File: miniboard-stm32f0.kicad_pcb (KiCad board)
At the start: 2 copper layers, 44 x 18.5 mm, 21 parts, among them P1 CONN_01X02, P2 CONN_01X13, P3 CONN_01X01, SW1 SW_PUSH, SW2 SW_PUSH, U1 stm32f030f4p6, Y1 8MHz

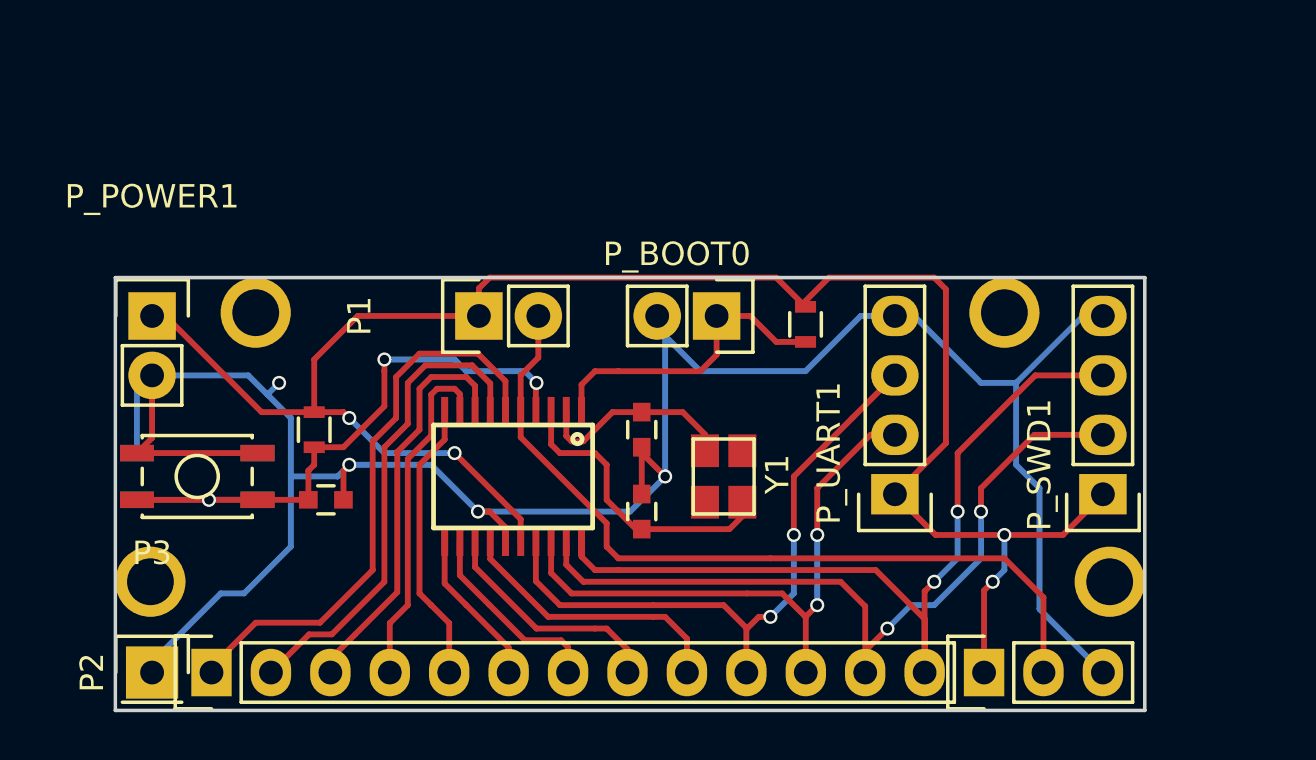
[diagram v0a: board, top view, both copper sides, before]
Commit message: Change quartz footprint, add text
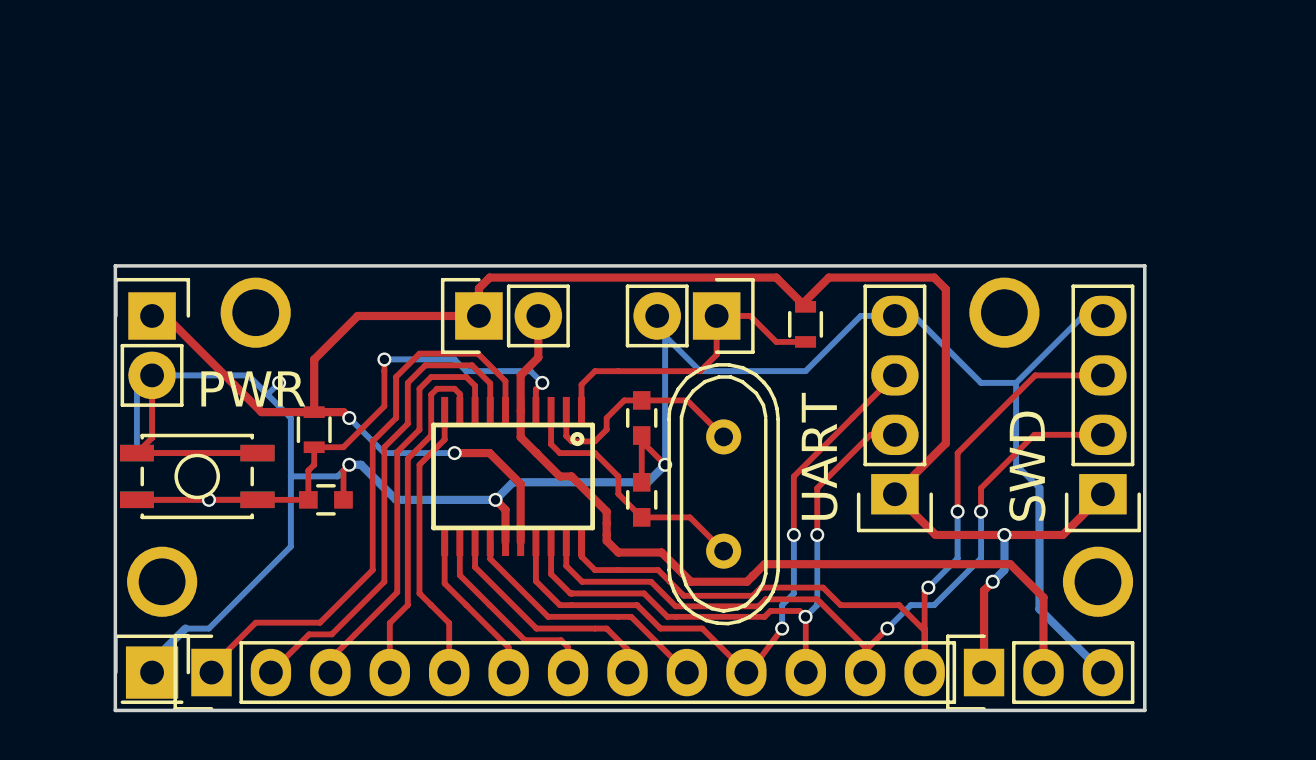
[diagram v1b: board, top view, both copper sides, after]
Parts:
- Y1: footprint Crystals:crystal_FA238-TSX3225 -> Crystals:Crystal_HC49-U_Vertical
- moved Y1 0.75 mm to (140.0, 111.8)
- moved C1 0.50 mm to (136.5, 108.5)
- moved C2 0.50 mm to (136.5, 112.0)
- moved H2 0.50 mm to (156.0, 115.5)
- moved H4 0.50 mm to (116.0, 115.5)
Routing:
- net /OSC_OUT: track 13.4 -> 11.4 mm
- net +3V3: track 79.4 -> 80.2 mm
- net /OSC_IN: track 8.70 -> 9.56 mm
- net /PB1: track 12.0 -> 11.1 mm
- net VAA: track 34.5 -> 35.2 mm
- net /PA13_SWDIO: track 35.3 -> 34.6 mm
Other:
- board size 44 x 18.5 mm -> 44 x 19 mm
- net class power added: clearance 0.2, trace_width 0.35, via_dia 0.6, via_drill 0.4
- board text added: "3.3"
- board text added: "3.3 VDD"
- board text added: "3.3V"
- board text added: "BOOT0"
- board text added: "FLASH"
- board text added: "GND"
- board text added: "PA0"
- board text added: "PA1"
- board text added: "PA10"
- board text added: "PA13"
- board text added: "PA14"
- board text added: "PA2"
- board text added: "PA3"
- board text added: "PA4"
- board text added: "PA5"
- board text added: "PA6"
- board text added: "PA7"
- board text added: "PA9"
- board text added: "PB1"
- board text added: "PWR"
- board text added: "RAM"
- board text added: "RST"
- board text added: "RX"
- board text added: "SWCLK"
- board text added: "SWD"
- board text added: "SWDIO"
- board text added: "TX"
- board text added: "UART"
- board text added: "VDDA"

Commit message: Add oshw logo Generate missing gerber files
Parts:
- added G***: LOGO, oshw:logo_xs, F.Cu at (124.2, 105.9)
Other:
- board text removed: "PWR"

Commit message: move logo
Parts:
- moved G*** 1.37 mm to (124.7, 104.6)
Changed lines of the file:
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@@
     (links 51)
     (no_connects 0)
-    (area 113.924999 101.924999 158.075001 121.075001)
+    (area 110.461667 97.915 161.318334 126.393095)
     (thickness 1.6)
     (drawings 46)
@@
   )
   (module oshw:logo_xs (layer F.Cu)
-    (at 124.206 105.918)
+    (at 124.714 104.648)
     (fp_text reference G*** (at 0 0) (layer F.SilkS) hide
       (effects (font (thickness 0.3)))

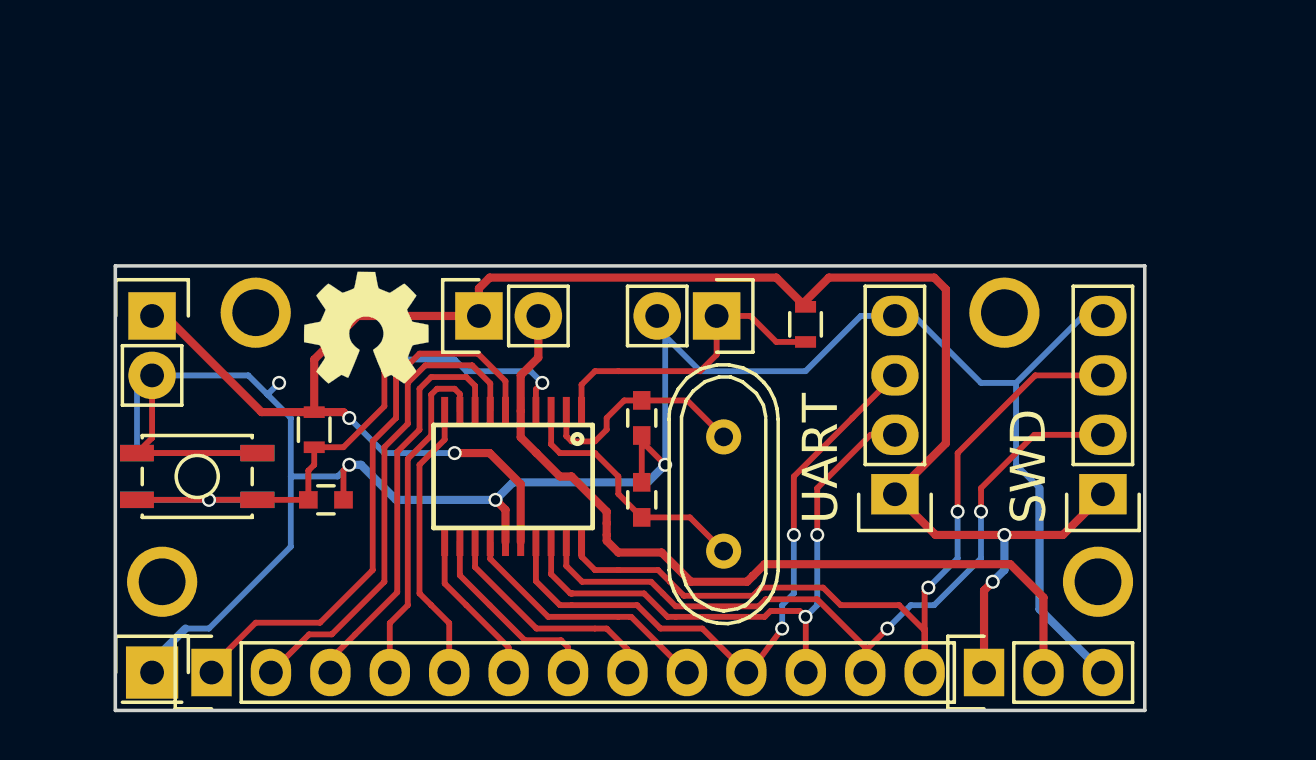
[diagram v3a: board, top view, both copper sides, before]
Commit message: * Use edge connector for SWD and uart connector * Add power LED * Fix reset button footprint * Add decoupling caps * Realign power connector
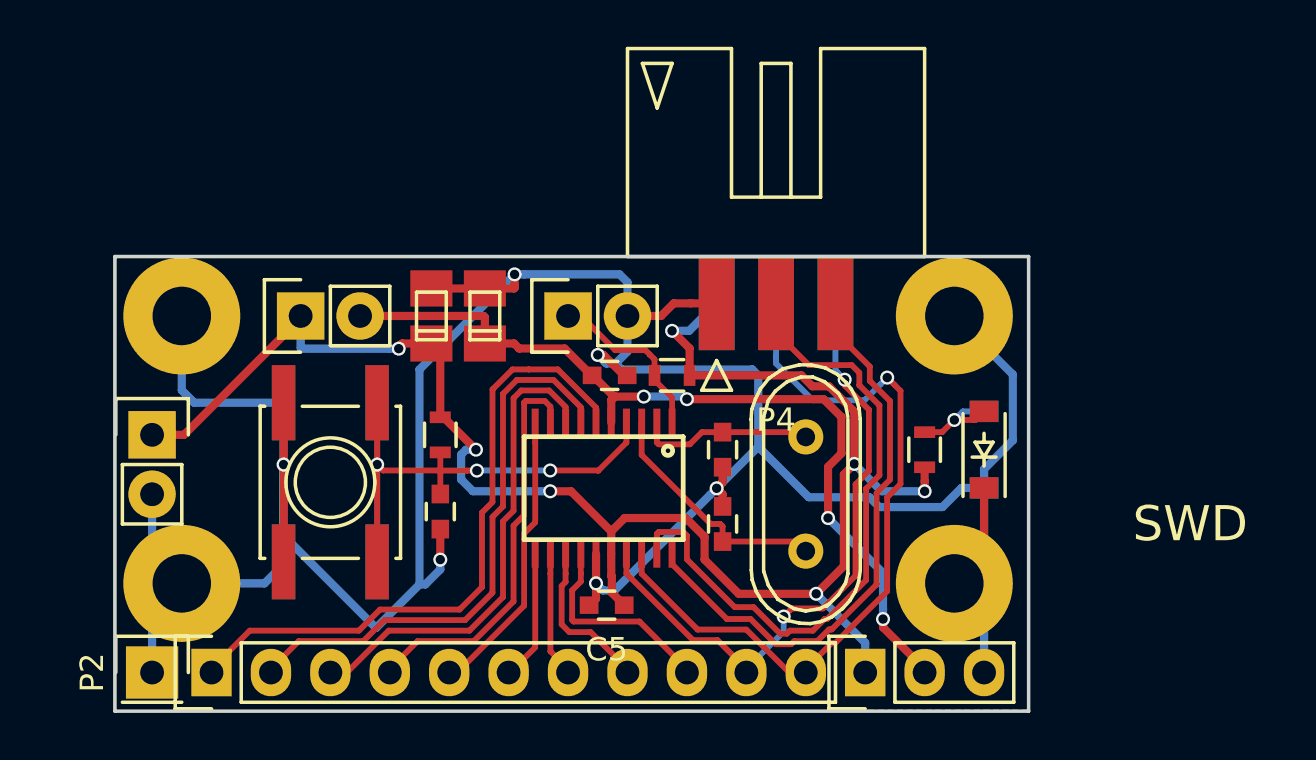
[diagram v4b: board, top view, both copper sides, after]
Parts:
- removed G***: LOGO, oshw:logo_xs
- removed P_SWD1, P_UART1: CONN_01X04, Pin_Headers:Pin_Header_Straight_1x04
- added C4: 4.7uF, Capacitors_Tantalum_SMD:TantalC_SizeR_EIA-2012, F.Cu at (127.5, 104.1)
- added C5: 100pF, Capacitors_SMD:C_0603, F.Cu at (135.0, 116.5)
- added C6: 1uF, Capacitors_Tantalum_SMD:TantalC_SizeR_EIA-2012, F.Cu at (129.8, 104.1)
- added C7: 10pF, Capacitors_SMD:C_0603, F.Cu at (135.1, 106.7)
- added D1: LED, Diodes_SMD:SOD-123, B.Cu at (151.1, 109.9)
- added D2: LED, Diodes_SMD:SOD-123, F.Cu at (151.1, 109.9)
- added P4: CONN_02X03, edge_connectors:pin_header_edge_6, F.Cu at (142.2, 101.6)
- added R3: 4.7k, Resistors_SMD:R_0603, F.Cu at (148.6, 109.9)
- H1, H2, H3, H4: footprint mechanics:hole_2mm -> mechanics:hole_2.5mm
- P2: value CONN_01X13 -> CONN_01X11; footprint Pin_Headers:Pin_Header_Straight_1x13 -> Pin_Headers:Pin_Header_Straight_1x11
- SW1, SW2: footprint Buttons_Switches_SMD:SW_SPST_EVQP2 -> Buttons_Switches_SMD:SW_SPST_EVQQ2
- moved P1 7.62 mm to (121.9, 104.1)
- moved P_BOOT0 6.35 mm to (133.3, 104.1), turned to 90 degrees
- moved H2 6.14 mm to (149.9, 115.6)
- moved R1 6.11 mm to (137.8, 106.7), turned to 180 degrees
- moved SW1 5.70 mm to (123.2, 111.2), turned to 90 degrees
- moved SW2 5.70 mm to (123.2, 111.2), turned to 270 degrees
- moved R2 5.39 mm to (127.9, 109.2)
- moved P_POWER1 5.08 mm to (115.6, 109.2)
- moved P_POWER_BOARD1 5.08 mm to (146.1, 119.4)
- moved C3 4.91 mm to (127.9, 112.5), turned to 270 degrees
- moved U1 3.90 mm to (134.9, 111.5)
- moved C1 3.71 mm to (140.0, 109.9)
- moved C2 3.60 mm to (140.0, 113.0)
- moved Y1 3.51 mm to (143.5, 111.8)
- moved H1 3.16 mm to (116.8, 104.1)
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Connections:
- H1 pad 1: Net-(H1-Pad1) -> GND
- H2 pad 1: Net-(H2-Pad1) -> GND
- H3 pad 1: Net-(H3-Pad1) -> GND
- H4 pad 1: Net-(H4-Pad1) -> GND
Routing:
- net GND: track 108.1 -> 141.0 mm, vias 4 -> 6
- net /PA14_SWCLK: track 36.5 -> 24.9 mm, vias 2 -> 0
- net /PA10_RX: track 25.6 -> 32.9 mm, vias 2 -> 1
- net /PA13_SWDIO: track 34.6 -> 28.1 mm, vias 2 -> 0
- net /BOOT0: track 13.9 -> 7.48 mm
- net +3V3: track 80.2 -> 74.2 mm, vias 4 -> 7
- net Net-(D1-Pad2): track 0.00 -> 4.33 mm, vias 0 -> 1
- net /PA1: track 20.7 -> 24.4 mm
- net /NRST: track 31.1 -> 27.5 mm
- net /PA0: track 24.4 -> 27.9 mm
- net /PA2: track 17.5 -> 20.8 mm
- net /PA7: track 10.0 -> 6.85 mm
- net /PA6: track 8.40 -> 5.39 mm
- net /PA3: track 14.8 -> 17.6 mm
- net /PB1: track 11.1 -> 8.91 mm
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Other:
- board size 44 x 19 mm -> 39.1 x 19.4 mm
- board text removed: "PA10"
- board text removed: "PA13"
- board text removed: "PA14"
- board text removed: "PB1"
- board text removed: "RST"
- board text removed: "SWCLK"
- board text removed: "UART"

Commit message: Fix minor routing issues Redraw mask
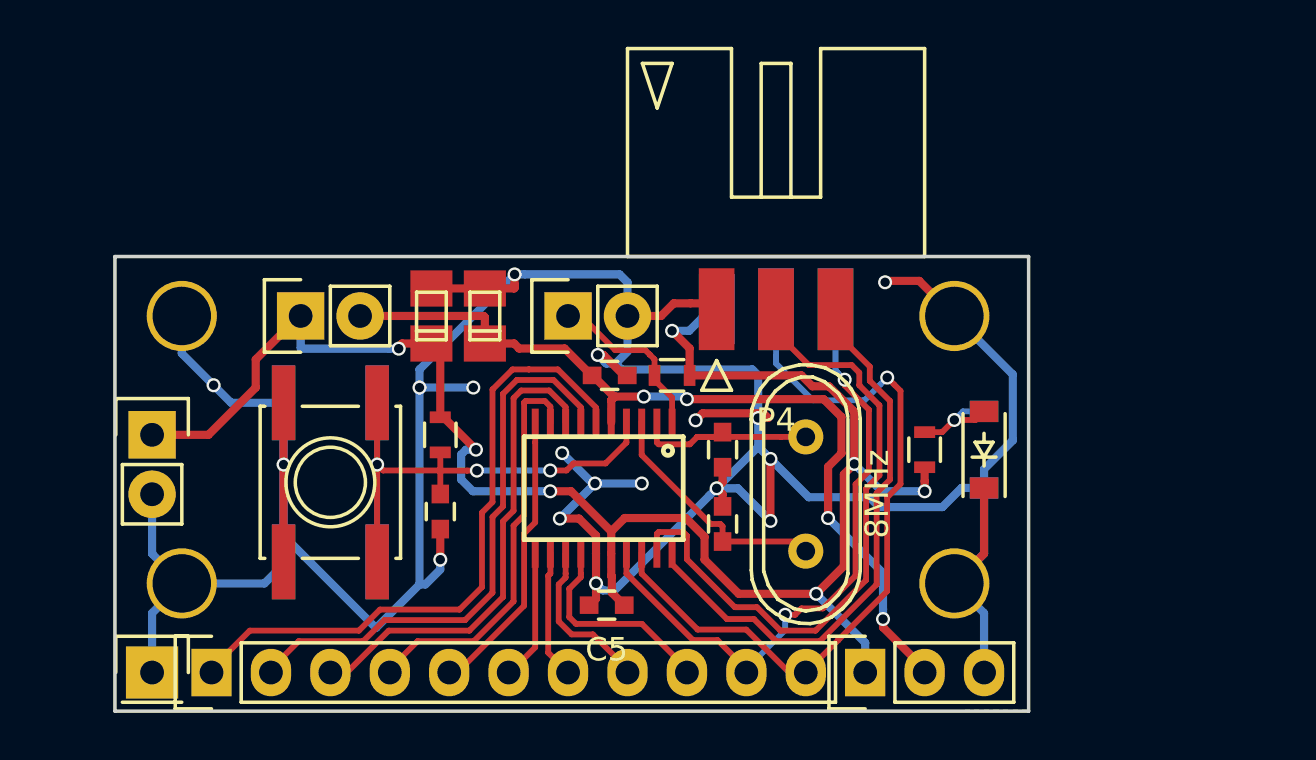
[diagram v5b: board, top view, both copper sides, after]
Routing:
- net GND: track 141.0 -> 163.9 mm, vias 6 -> 18
- net /OSC_IN: track 7.55 -> 8.57 mm
- net +3V3: track 74.2 -> 74.8 mm
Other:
- board text added: "A0"
- board text added: "A1"
- board text added: "A10"
- board text added: "A2"
- board text added: "A3"
- board text added: "A4"
- board text added: "A5"
- board text added: "A6"
- board text added: "A7"
- board text added: "A9"
- board text added: "B1"
- board text added: "G"
- board text added: "RESET"
- board text added: "SWCLK"
- board text added: "UART_RX"
- board text added: "UART_TX"
- board text removed: "3.3 VDD"
- board text removed: "PA0"
- board text removed: "PA1"
- board text removed: "PA2"
- board text removed: "PA3"
- board text removed: "PA4"
- board text removed: "PA5"
- board text removed: "PA6"
- board text removed: "PA7"
- board text removed: "PA9"
- board text removed: "RX"
- board text removed: "SWD"
- board text removed: "TX"
